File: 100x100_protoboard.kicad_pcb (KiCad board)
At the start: 2 copper layers, 0 parts

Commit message: completed first beta-version of the composite board
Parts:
- added C1: u33, Capacitors_SMD:C_0805_HandSoldering, B.Cu at (66.5, 125.2)
- added C1: u33, Capacitors_SMD:C_0805_HandSoldering, B.Cu at (107.2, 125.2)
- added C1: u33, Capacitors_SMD:C_0805_HandSoldering, B.Cu at (66.6, 33.3)
- added C1: u33, Capacitors_SMD:C_0805_HandSoldering, B.Cu at (107.2, 33.3)
- added C2: u1, Capacitors_SMD:C_0805_HandSoldering, B.Cu at (69.1, 125.2)
- added C2: u1, Capacitors_SMD:C_0805_HandSoldering, B.Cu at (104.6, 125.2)
- added C2: u1, Capacitors_SMD:C_0805_HandSoldering, B.Cu at (69.1, 33.3)
- added C2: u1, Capacitors_SMD:C_0805_HandSoldering, B.Cu at (104.6, 33.3)
- added CON1: BARREL_JACK, Connect:BARREL_JACK, B.Cu at (40.4, 125.0)
- added CON1: BARREL_JACK, Connect:BARREL_JACK, F.Cu at (133.2, 125.0)
- added CON1: BARREL_JACK, Connect:BARREL_JACK, F.Cu at (40.5, 33.5)
- added CON1: BARREL_JACK, Connect:BARREL_JACK, B.Cu at (133.3, 33.5)
- added CON2: USB_FEMALE_WITH_ID, Connectors:USB_Mini-B_Female, F.Cu at (132.0, 103.4)
- added CON2: USB_FEMALE_WITH_ID, Connectors:USB_Mini-B_Female, F.Cu at (41.8, 55.1)
- added CON3: USB_FEMALE_WITH_ID, Connectors:USB_Micro-B_Female_Wellco_AUSB_1011_05S2, B.Cu at (132.1, 103.4)
- added CON3: USB_FEMALE_WITH_ID, Connectors:USB_Micro-B_Female_Wellco_AUSB_1011_05S2, B.Cu at (41.7, 55.1)
- added F1: FUSE, Muonde:CC12ZZ, B.Cu at (51.3, 125.0)
- added F1: FUSE, Muonde:CC12ZZ, F.Cu at (122.4, 125.0)
- added F1: FUSE, Muonde:CC12ZZ, F.Cu at (51.3, 33.5)
- added F1: FUSE, Muonde:CC12ZZ, B.Cu at (122.4, 33.5)
- added F2: FUSE, Muonde:CC12ZZ, F.Cu at (51.3, 125.0)
- added F2: FUSE, Muonde:CC12ZZ, B.Cu at (122.4, 125.0)
- added F2: FUSE, Muonde:CC12ZZ, B.Cu at (51.3, 33.5)
- added F2: FUSE, Muonde:CC12ZZ, F.Cu at (122.4, 33.5)
- added GND1: INTERCONNECT_1X16, 2.54mm_Pin_Headers:Interconnect_1x16, F.Cu at (47.5, 121.2)
- added GND1: INTERCONNECT_1X16, 2.54mm_Pin_Headers:Interconnect_1x16, F.Cu at (126.2, 83.1)
- added GND1: INTERCONNECT_1X16, 2.54mm_Pin_Headers:Interconnect_1x16, F.Cu at (47.5, 75.4)
- added GND1: INTERCONNECT_1X16, 2.54mm_Pin_Headers:Interconnect_1x16, F.Cu at (126.2, 37.3)
- added GND2: INTERCONNECT_1X07, 2.54mm_Pin_Headers:Interconnect_1x07, F.Cu at (47.5, 80.5)
- added GND2: INTERCONNECT_1X07, 2.54mm_Pin_Headers:Interconnect_1x07, F.Cu at (126.2, 80.5)
- added GND2: INTERCONNECT_1X07, 2.54mm_Pin_Headers:Interconnect_1x07, F.Cu at (47.5, 78.0)
- added GND2: INTERCONNECT_1X07, 2.54mm_Pin_Headers:Interconnect_1x07, F.Cu at (126.2, 78.0)
- added GND3: INTERCONNECT_1X16, 2.54mm_Pin_Headers:Interconnect_1x16, F.Cu at (67.8, 121.2)
- added GND3: INTERCONNECT_1X16, 2.54mm_Pin_Headers:Interconnect_1x16, F.Cu at (105.9, 83.1)
- added GND3: INTERCONNECT_1X16, 2.54mm_Pin_Headers:Interconnect_1x16, F.Cu at (67.8, 75.4)
- added GND3: INTERCONNECT_1X16, 2.54mm_Pin_Headers:Interconnect_1x16, F.Cu at (105.9, 37.3)
- added GND4: INTERCONNECT_1X07, 2.54mm_Pin_Headers:Interconnect_1x07, F.Cu at (67.8, 80.5)
- added GND4: INTERCONNECT_1X07, 2.54mm_Pin_Headers:Interconnect_1x07, F.Cu at (105.9, 80.5)
- added GND4: INTERCONNECT_1X07, 2.54mm_Pin_Headers:Interconnect_1x07, F.Cu at (67.8, 78.0)
- added GND4: INTERCONNECT_1X07, 2.54mm_Pin_Headers:Interconnect_1x07, F.Cu at (105.9, 78.0)
- added J1: INTERCONNECT_1X03, 2.54mm_Pin_Headers:Interconnect_1x03, F.Cu at (50.0, 121.2)
- added J1: INTERCONNECT_1X03, 2.54mm_Pin_Headers:Interconnect_1x03, F.Cu at (123.7, 121.2)
- added J1: INTERCONNECT_1X03, 2.54mm_Pin_Headers:Interconnect_1x03, F.Cu at (50.0, 37.3)
- added J1: INTERCONNECT_1X03, 2.54mm_Pin_Headers:Interconnect_1x03, F.Cu at (123.7, 37.3)
- added J10: INTERCONNECT_1X03, 2.54mm_Pin_Headers:Interconnect_1x03, F.Cu at (50.0, 98.3)
- added J10: INTERCONNECT_1X03, 2.54mm_Pin_Headers:Interconnect_1x03, F.Cu at (123.7, 98.3)
- added J10: INTERCONNECT_1X03, 2.54mm_Pin_Headers:Interconnect_1x03, F.Cu at (50.0, 60.2)
- added J10: INTERCONNECT_1X03, 2.54mm_Pin_Headers:Interconnect_1x03, F.Cu at (123.7, 60.2)
- added J11: INTERCONNECT_1X03, 2.54mm_Pin_Headers:Interconnect_1x03, F.Cu at (50.0, 95.8)
- added J11: INTERCONNECT_1X03, 2.54mm_Pin_Headers:Interconnect_1x03, F.Cu at (123.7, 95.8)
- added J11: INTERCONNECT_1X03, 2.54mm_Pin_Headers:Interconnect_1x03, F.Cu at (50.0, 62.7)
- added J11: INTERCONNECT_1X03, 2.54mm_Pin_Headers:Interconnect_1x03, F.Cu at (123.7, 62.7)
- added J12: INTERCONNECT_1X03, 2.54mm_Pin_Headers:Interconnect_1x03, F.Cu at (50.0, 93.2)
- added J12: INTERCONNECT_1X03, 2.54mm_Pin_Headers:Interconnect_1x03, F.Cu at (123.7, 93.2)
- added J12: INTERCONNECT_1X03, 2.54mm_Pin_Headers:Interconnect_1x03, F.Cu at (50.0, 65.3)
- added J12: INTERCONNECT_1X03, 2.54mm_Pin_Headers:Interconnect_1x03, F.Cu at (123.7, 65.3)
- added J13: INTERCONNECT_1X03, 2.54mm_Pin_Headers:Interconnect_1x03, F.Cu at (50.0, 90.7)
- added J13: INTERCONNECT_1X03, 2.54mm_Pin_Headers:Interconnect_1x03, F.Cu at (123.7, 90.7)
- added J13: INTERCONNECT_1X03, 2.54mm_Pin_Headers:Interconnect_1x03, F.Cu at (50.0, 67.8)
- added J13: INTERCONNECT_1X03, 2.54mm_Pin_Headers:Interconnect_1x03, F.Cu at (123.7, 67.8)
- added J14: INTERCONNECT_1X03, 2.54mm_Pin_Headers:Interconnect_1x03, F.Cu at (50.0, 88.1)
- added J14: INTERCONNECT_1X03, 2.54mm_Pin_Headers:Interconnect_1x03, F.Cu at (123.7, 88.1)
- added J14: INTERCONNECT_1X03, 2.54mm_Pin_Headers:Interconnect_1x03, F.Cu at (50.0, 70.4)
- added J14: INTERCONNECT_1X03, 2.54mm_Pin_Headers:Interconnect_1x03, F.Cu at (123.7, 70.4)
- added J15: INTERCONNECT_1X03, 2.54mm_Pin_Headers:Interconnect_1x03, F.Cu at (50.0, 85.6)
- added J15: INTERCONNECT_1X03, 2.54mm_Pin_Headers:Interconnect_1x03, F.Cu at (123.7, 85.6)
- added J15: INTERCONNECT_1X03, 2.54mm_Pin_Headers:Interconnect_1x03, F.Cu at (50.0, 72.9)
- added J15: INTERCONNECT_1X03, 2.54mm_Pin_Headers:Interconnect_1x03, F.Cu at (123.7, 72.9)
- added J16: INTERCONNECT_1X03, 2.54mm_Pin_Headers:Interconnect_1x03, F.Cu at (50.0, 83.1)
- added J16: INTERCONNECT_1X03, 2.54mm_Pin_Headers:Interconnect_1x03, F.Cu at (123.7, 83.1)
- added J16: INTERCONNECT_1X03, 2.54mm_Pin_Headers:Interconnect_1x03, F.Cu at (50.0, 75.4)
- added J16: INTERCONNECT_1X03, 2.54mm_Pin_Headers:Interconnect_1x03, F.Cu at (123.7, 75.4)
- added J17: INTERCONNECT_1X03, 2.54mm_Pin_Headers:Interconnect_1x03, F.Cu at (57.7, 121.2)
- added J17: INTERCONNECT_1X03, 2.54mm_Pin_Headers:Interconnect_1x03, F.Cu at (116.1, 121.2)
- added J17: INTERCONNECT_1X03, 2.54mm_Pin_Headers:Interconnect_1x03, F.Cu at (57.7, 37.3)
- added J17: INTERCONNECT_1X03, 2.54mm_Pin_Headers:Interconnect_1x03, F.Cu at (116.1, 37.3)
- added J18: INTERCONNECT_1X03, 2.54mm_Pin_Headers:Interconnect_1x03, F.Cu at (57.7, 118.6)
- added J18: INTERCONNECT_1X03, 2.54mm_Pin_Headers:Interconnect_1x03, F.Cu at (116.1, 118.6)
- added J18: INTERCONNECT_1X03, 2.54mm_Pin_Headers:Interconnect_1x03, F.Cu at (57.7, 39.9)
- added J18: INTERCONNECT_1X03, 2.54mm_Pin_Headers:Interconnect_1x03, F.Cu at (116.1, 39.9)
- added J19: INTERCONNECT_1X03, 2.54mm_Pin_Headers:Interconnect_1x03, F.Cu at (57.7, 116.1)
- added J19: INTERCONNECT_1X03, 2.54mm_Pin_Headers:Interconnect_1x03, F.Cu at (116.1, 116.1)
- added J19: INTERCONNECT_1X03, 2.54mm_Pin_Headers:Interconnect_1x03, F.Cu at (57.7, 42.4)
- added J19: INTERCONNECT_1X03, 2.54mm_Pin_Headers:Interconnect_1x03, F.Cu at (116.1, 42.4)
- added J2: INTERCONNECT_1X03, 2.54mm_Pin_Headers:Interconnect_1x03, F.Cu at (50.0, 118.6)
- added J2: INTERCONNECT_1X03, 2.54mm_Pin_Headers:Interconnect_1x03, F.Cu at (123.7, 118.6)
- added J2: INTERCONNECT_1X03, 2.54mm_Pin_Headers:Interconnect_1x03, F.Cu at (50.0, 39.9)
- added J2: INTERCONNECT_1X03, 2.54mm_Pin_Headers:Interconnect_1x03, F.Cu at (123.7, 39.9)
- added J20: INTERCONNECT_1X03, 2.54mm_Pin_Headers:Interconnect_1x03, F.Cu at (57.7, 113.5)
- added J20: INTERCONNECT_1X03, 2.54mm_Pin_Headers:Interconnect_1x03, F.Cu at (116.1, 113.5)
- added J20: INTERCONNECT_1X03, 2.54mm_Pin_Headers:Interconnect_1x03, F.Cu at (57.7, 45.0)
- added J20: INTERCONNECT_1X03, 2.54mm_Pin_Headers:Interconnect_1x03, F.Cu at (116.1, 45.0)
- added J21: INTERCONNECT_1X03, 2.54mm_Pin_Headers:Interconnect_1x03, F.Cu at (57.7, 111.0)
- added J21: INTERCONNECT_1X03, 2.54mm_Pin_Headers:Interconnect_1x03, F.Cu at (116.1, 111.0)
- added J21: INTERCONNECT_1X03, 2.54mm_Pin_Headers:Interconnect_1x03, F.Cu at (57.7, 47.5)
- added J21: INTERCONNECT_1X03, 2.54mm_Pin_Headers:Interconnect_1x03, F.Cu at (116.1, 47.5)
- added J22: INTERCONNECT_1X03, 2.54mm_Pin_Headers:Interconnect_1x03, F.Cu at (57.7, 108.5)
- added J22: INTERCONNECT_1X03, 2.54mm_Pin_Headers:Interconnect_1x03, F.Cu at (116.1, 108.5)
- added J22: INTERCONNECT_1X03, 2.54mm_Pin_Headers:Interconnect_1x03, F.Cu at (57.7, 50.0)
- added J22: INTERCONNECT_1X03, 2.54mm_Pin_Headers:Interconnect_1x03, F.Cu at (116.1, 50.0)
- added J23: INTERCONNECT_1X03, 2.54mm_Pin_Headers:Interconnect_1x03, F.Cu at (57.7, 105.9)
- added J23: INTERCONNECT_1X03, 2.54mm_Pin_Headers:Interconnect_1x03, F.Cu at (116.1, 105.9)
- added J23: INTERCONNECT_1X03, 2.54mm_Pin_Headers:Interconnect_1x03, F.Cu at (57.7, 52.6)
- added J23: INTERCONNECT_1X03, 2.54mm_Pin_Headers:Interconnect_1x03, F.Cu at (116.1, 52.6)
- added J24: INTERCONNECT_1X03, 2.54mm_Pin_Headers:Interconnect_1x03, F.Cu at (57.7, 103.4)
- added J24: INTERCONNECT_1X03, 2.54mm_Pin_Headers:Interconnect_1x03, F.Cu at (116.1, 103.4)
- added J24: INTERCONNECT_1X03, 2.54mm_Pin_Headers:Interconnect_1x03, F.Cu at (57.7, 55.1)
- added J24: INTERCONNECT_1X03, 2.54mm_Pin_Headers:Interconnect_1x03, F.Cu at (116.1, 55.1)
- added J25: INTERCONNECT_1X03, 2.54mm_Pin_Headers:Interconnect_1x03, F.Cu at (57.7, 100.8)
- added J25: INTERCONNECT_1X03, 2.54mm_Pin_Headers:Interconnect_1x03, F.Cu at (116.1, 100.8)
- added J25: INTERCONNECT_1X03, 2.54mm_Pin_Headers:Interconnect_1x03, F.Cu at (57.7, 57.7)
- added J25: INTERCONNECT_1X03, 2.54mm_Pin_Headers:Interconnect_1x03, F.Cu at (116.1, 57.7)
- added J26: INTERCONNECT_1X03, 2.54mm_Pin_Headers:Interconnect_1x03, F.Cu at (57.7, 98.3)
- added J26: INTERCONNECT_1X03, 2.54mm_Pin_Headers:Interconnect_1x03, F.Cu at (116.1, 98.3)
- added J26: INTERCONNECT_1X03, 2.54mm_Pin_Headers:Interconnect_1x03, F.Cu at (57.7, 60.2)
- added J26: INTERCONNECT_1X03, 2.54mm_Pin_Headers:Interconnect_1x03, F.Cu at (116.1, 60.2)
- added J27: INTERCONNECT_1X03, 2.54mm_Pin_Headers:Interconnect_1x03, F.Cu at (57.7, 95.8)
- added J27: INTERCONNECT_1X03, 2.54mm_Pin_Headers:Interconnect_1x03, F.Cu at (116.1, 95.8)
- added J27: INTERCONNECT_1X03, 2.54mm_Pin_Headers:Interconnect_1x03, F.Cu at (57.7, 62.7)
- added J27: INTERCONNECT_1X03, 2.54mm_Pin_Headers:Interconnect_1x03, F.Cu at (116.1, 62.7)
- added J28: INTERCONNECT_1X03, 2.54mm_Pin_Headers:Interconnect_1x03, F.Cu at (57.7, 93.2)
- added J28: INTERCONNECT_1X03, 2.54mm_Pin_Headers:Interconnect_1x03, F.Cu at (116.1, 93.2)
- added J28: INTERCONNECT_1X03, 2.54mm_Pin_Headers:Interconnect_1x03, F.Cu at (57.7, 65.3)
- added J28: INTERCONNECT_1X03, 2.54mm_Pin_Headers:Interconnect_1x03, F.Cu at (116.1, 65.3)
- added J29: INTERCONNECT_1X03, 2.54mm_Pin_Headers:Interconnect_1x03, F.Cu at (57.7, 90.7)
- added J29: INTERCONNECT_1X03, 2.54mm_Pin_Headers:Interconnect_1x03, F.Cu at (116.1, 90.7)
- added J29: INTERCONNECT_1X03, 2.54mm_Pin_Headers:Interconnect_1x03, F.Cu at (57.7, 67.8)
- added J29: INTERCONNECT_1X03, 2.54mm_Pin_Headers:Interconnect_1x03, F.Cu at (116.1, 67.8)
- added J3: INTERCONNECT_1X03, 2.54mm_Pin_Headers:Interconnect_1x03, F.Cu at (50.0, 116.1)
- added J3: INTERCONNECT_1X03, 2.54mm_Pin_Headers:Interconnect_1x03, F.Cu at (123.7, 116.1)
- added J3: INTERCONNECT_1X03, 2.54mm_Pin_Headers:Interconnect_1x03, F.Cu at (50.0, 42.4)
- added J3: INTERCONNECT_1X03, 2.54mm_Pin_Headers:Interconnect_1x03, F.Cu at (123.7, 42.4)
- added J30: INTERCONNECT_1X03, 2.54mm_Pin_Headers:Interconnect_1x03, F.Cu at (57.7, 88.1)
- added J30: INTERCONNECT_1X03, 2.54mm_Pin_Headers:Interconnect_1x03, F.Cu at (116.1, 88.1)
- added J30: INTERCONNECT_1X03, 2.54mm_Pin_Headers:Interconnect_1x03, F.Cu at (57.7, 70.4)
- added J30: INTERCONNECT_1X03, 2.54mm_Pin_Headers:Interconnect_1x03, F.Cu at (116.1, 70.4)
- added J31: INTERCONNECT_1X03, 2.54mm_Pin_Headers:Interconnect_1x03, F.Cu at (57.7, 85.6)
- added J31: INTERCONNECT_1X03, 2.54mm_Pin_Headers:Interconnect_1x03, F.Cu at (116.1, 85.6)
- added J31: INTERCONNECT_1X03, 2.54mm_Pin_Headers:Interconnect_1x03, F.Cu at (57.7, 72.9)
- added J31: INTERCONNECT_1X03, 2.54mm_Pin_Headers:Interconnect_1x03, F.Cu at (116.1, 72.9)
- added J32: INTERCONNECT_1X03, 2.54mm_Pin_Headers:Interconnect_1x03, F.Cu at (57.7, 83.1)
- added J32: INTERCONNECT_1X03, 2.54mm_Pin_Headers:Interconnect_1x03, F.Cu at (116.1, 83.1)
- added J32: INTERCONNECT_1X03, 2.54mm_Pin_Headers:Interconnect_1x03, F.Cu at (57.7, 75.4)
- added J32: INTERCONNECT_1X03, 2.54mm_Pin_Headers:Interconnect_1x03, F.Cu at (116.1, 75.4)
- added J33: INTERCONNECT_1X03, 2.54mm_Pin_Headers:Interconnect_1x03, F.Cu at (70.4, 121.2)
- added J33: INTERCONNECT_1X03, 2.54mm_Pin_Headers:Interconnect_1x03, F.Cu at (103.4, 121.2)
- added J33: INTERCONNECT_1X03, 2.54mm_Pin_Headers:Interconnect_1x03, F.Cu at (70.4, 37.3)
- added J33: INTERCONNECT_1X03, 2.54mm_Pin_Headers:Interconnect_1x03, F.Cu at (103.4, 37.3)
- added J34: INTERCONNECT_1X03, 2.54mm_Pin_Headers:Interconnect_1x03, F.Cu at (70.4, 118.6)
- added J34: INTERCONNECT_1X03, 2.54mm_Pin_Headers:Interconnect_1x03, F.Cu at (103.4, 118.6)
- added J34: INTERCONNECT_1X03, 2.54mm_Pin_Headers:Interconnect_1x03, F.Cu at (70.4, 39.9)
- added J34: INTERCONNECT_1X03, 2.54mm_Pin_Headers:Interconnect_1x03, F.Cu at (103.4, 39.9)
- added J35: INTERCONNECT_1X03, 2.54mm_Pin_Headers:Interconnect_1x03, F.Cu at (70.4, 116.1)
- added J35: INTERCONNECT_1X03, 2.54mm_Pin_Headers:Interconnect_1x03, F.Cu at (103.4, 116.1)
- added J35: INTERCONNECT_1X03, 2.54mm_Pin_Headers:Interconnect_1x03, F.Cu at (70.4, 42.4)
- added J35: INTERCONNECT_1X03, 2.54mm_Pin_Headers:Interconnect_1x03, F.Cu at (103.4, 42.4)
- added J36: INTERCONNECT_1X03, 2.54mm_Pin_Headers:Interconnect_1x03, F.Cu at (70.4, 113.5)
- added J36: INTERCONNECT_1X03, 2.54mm_Pin_Headers:Interconnect_1x03, F.Cu at (103.4, 113.5)
- added J36: INTERCONNECT_1X03, 2.54mm_Pin_Headers:Interconnect_1x03, F.Cu at (70.4, 45.0)
- added J36: INTERCONNECT_1X03, 2.54mm_Pin_Headers:Interconnect_1x03, F.Cu at (103.4, 45.0)
- added J37: INTERCONNECT_1X03, 2.54mm_Pin_Headers:Interconnect_1x03, F.Cu at (70.4, 111.0)
- added J37: INTERCONNECT_1X03, 2.54mm_Pin_Headers:Interconnect_1x03, F.Cu at (103.4, 111.0)
- added J37: INTERCONNECT_1X03, 2.54mm_Pin_Headers:Interconnect_1x03, F.Cu at (70.4, 47.5)
- added J37: INTERCONNECT_1X03, 2.54mm_Pin_Headers:Interconnect_1x03, F.Cu at (103.4, 47.5)
- added J38: INTERCONNECT_1X03, 2.54mm_Pin_Headers:Interconnect_1x03, F.Cu at (70.4, 108.5)
- added J38: INTERCONNECT_1X03, 2.54mm_Pin_Headers:Interconnect_1x03, F.Cu at (103.4, 108.5)
- added J38: INTERCONNECT_1X03, 2.54mm_Pin_Headers:Interconnect_1x03, F.Cu at (70.4, 50.0)
- added J38: INTERCONNECT_1X03, 2.54mm_Pin_Headers:Interconnect_1x03, F.Cu at (103.4, 50.0)
- added J39: INTERCONNECT_1X03, 2.54mm_Pin_Headers:Interconnect_1x03, F.Cu at (70.4, 105.9)
- added J39: INTERCONNECT_1X03, 2.54mm_Pin_Headers:Interconnect_1x03, F.Cu at (103.4, 105.9)
- added J39: INTERCONNECT_1X03, 2.54mm_Pin_Headers:Interconnect_1x03, F.Cu at (70.4, 52.6)
- added J39: INTERCONNECT_1X03, 2.54mm_Pin_Headers:Interconnect_1x03, F.Cu at (103.4, 52.6)
- added J4: INTERCONNECT_1X03, 2.54mm_Pin_Headers:Interconnect_1x03, F.Cu at (50.0, 113.5)
- added J4: INTERCONNECT_1X03, 2.54mm_Pin_Headers:Interconnect_1x03, F.Cu at (123.7, 113.5)
- added J4: INTERCONNECT_1X03, 2.54mm_Pin_Headers:Interconnect_1x03, F.Cu at (50.0, 45.0)
- added J4: INTERCONNECT_1X03, 2.54mm_Pin_Headers:Interconnect_1x03, F.Cu at (123.7, 45.0)
- added J40: INTERCONNECT_1X03, 2.54mm_Pin_Headers:Interconnect_1x03, F.Cu at (70.4, 103.4)
- added J40: INTERCONNECT_1X03, 2.54mm_Pin_Headers:Interconnect_1x03, F.Cu at (103.4, 103.4)
- added J40: INTERCONNECT_1X03, 2.54mm_Pin_Headers:Interconnect_1x03, F.Cu at (70.4, 55.1)
- added J40: INTERCONNECT_1X03, 2.54mm_Pin_Headers:Interconnect_1x03, F.Cu at (103.4, 55.1)
- added J41: INTERCONNECT_1X03, 2.54mm_Pin_Headers:Interconnect_1x03, F.Cu at (70.4, 100.8)
- added J41: INTERCONNECT_1X03, 2.54mm_Pin_Headers:Interconnect_1x03, F.Cu at (103.4, 100.8)
- added J41: INTERCONNECT_1X03, 2.54mm_Pin_Headers:Interconnect_1x03, F.Cu at (70.4, 57.7)
- added J41: INTERCONNECT_1X03, 2.54mm_Pin_Headers:Interconnect_1x03, F.Cu at (103.4, 57.7)
- added J42: INTERCONNECT_1X03, 2.54mm_Pin_Headers:Interconnect_1x03, F.Cu at (70.4, 98.3)
- added J42: INTERCONNECT_1X03, 2.54mm_Pin_Headers:Interconnect_1x03, F.Cu at (103.4, 98.3)
- added J42: INTERCONNECT_1X03, 2.54mm_Pin_Headers:Interconnect_1x03, F.Cu at (70.4, 60.2)
- added J42: INTERCONNECT_1X03, 2.54mm_Pin_Headers:Interconnect_1x03, F.Cu at (103.4, 60.2)
- added J43: INTERCONNECT_1X03, 2.54mm_Pin_Headers:Interconnect_1x03, F.Cu at (70.4, 95.8)
- added J43: INTERCONNECT_1X03, 2.54mm_Pin_Headers:Interconnect_1x03, F.Cu at (103.4, 95.8)
- added J43: INTERCONNECT_1X03, 2.54mm_Pin_Headers:Interconnect_1x03, F.Cu at (70.4, 62.7)
- added J43: INTERCONNECT_1X03, 2.54mm_Pin_Headers:Interconnect_1x03, F.Cu at (103.4, 62.7)
- added J44: INTERCONNECT_1X03, 2.54mm_Pin_Headers:Interconnect_1x03, F.Cu at (70.4, 93.2)
- added J44: INTERCONNECT_1X03, 2.54mm_Pin_Headers:Interconnect_1x03, F.Cu at (103.4, 93.2)
- added J44: INTERCONNECT_1X03, 2.54mm_Pin_Headers:Interconnect_1x03, F.Cu at (70.4, 65.3)
- added J44: INTERCONNECT_1X03, 2.54mm_Pin_Headers:Interconnect_1x03, F.Cu at (103.4, 65.3)
- added J45: INTERCONNECT_1X03, 2.54mm_Pin_Headers:Interconnect_1x03, F.Cu at (70.4, 90.7)
- added J45: INTERCONNECT_1X03, 2.54mm_Pin_Headers:Interconnect_1x03, F.Cu at (103.4, 90.7)
- added J45: INTERCONNECT_1X03, 2.54mm_Pin_Headers:Interconnect_1x03, F.Cu at (70.4, 67.8)
- added J45: INTERCONNECT_1X03, 2.54mm_Pin_Headers:Interconnect_1x03, F.Cu at (103.4, 67.8)
- added J46: INTERCONNECT_1X03, 2.54mm_Pin_Headers:Interconnect_1x03, F.Cu at (70.4, 88.1)
- added J46: INTERCONNECT_1X03, 2.54mm_Pin_Headers:Interconnect_1x03, F.Cu at (103.4, 88.1)
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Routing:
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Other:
- board outline added: 97.8 x 96.5 mm
- net class Power added: clearance 0.254, trace_width 2.032, via_dia 0.889, via_drill 0.635
- board text added: "100n"
- board text added: "330n"
- board text added: "78 XX"
- board text added: "D+"
- board text added: "D-"
- board text added: "FUSE"
- board text added: "GND"
- board text added: "ID"
- board text added: "POWER JACK"
- board text added: "PTC"
- board text added: "USB MICRO"
- board text added: "USB MINI"
- board text added: "VCC"

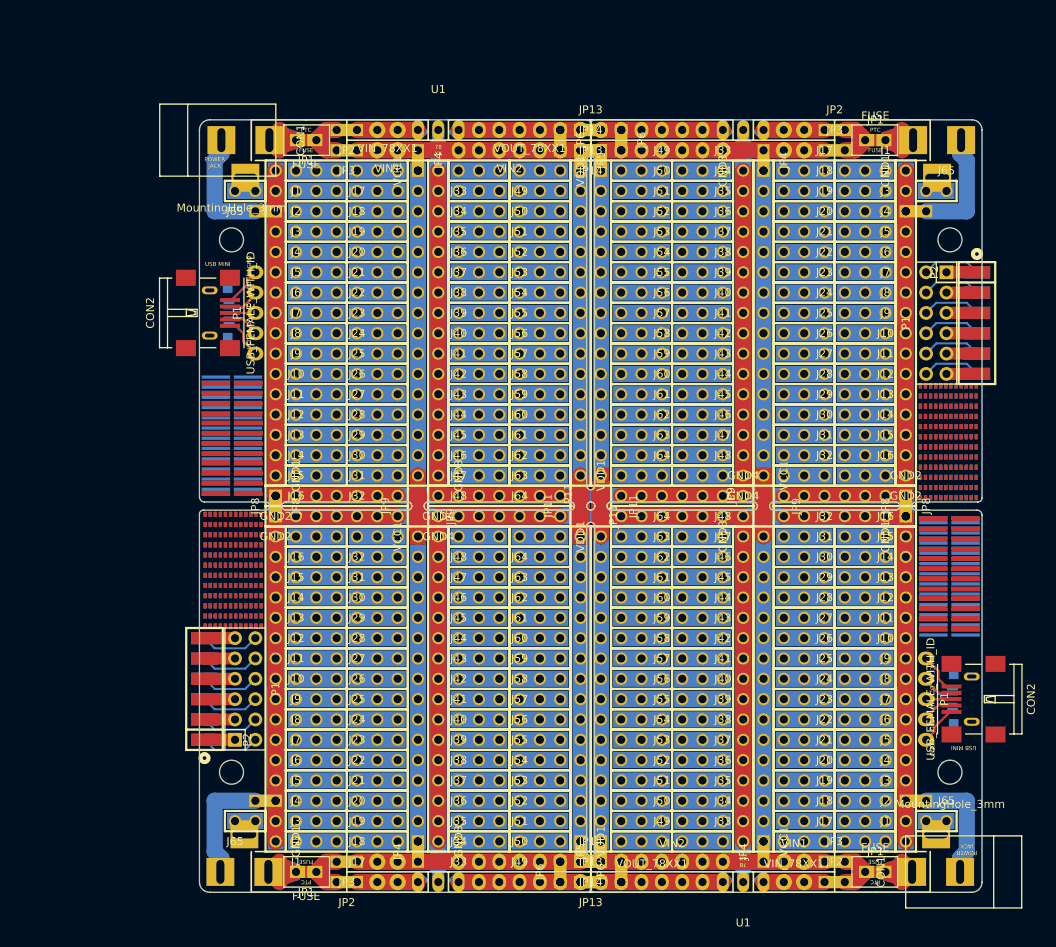
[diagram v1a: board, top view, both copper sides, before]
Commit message: moved shorted inter-board GND connection to center, switched av from Oddities:NetTie-I_Connected_SMD because they were asymmetrical and fixed pin header outlines
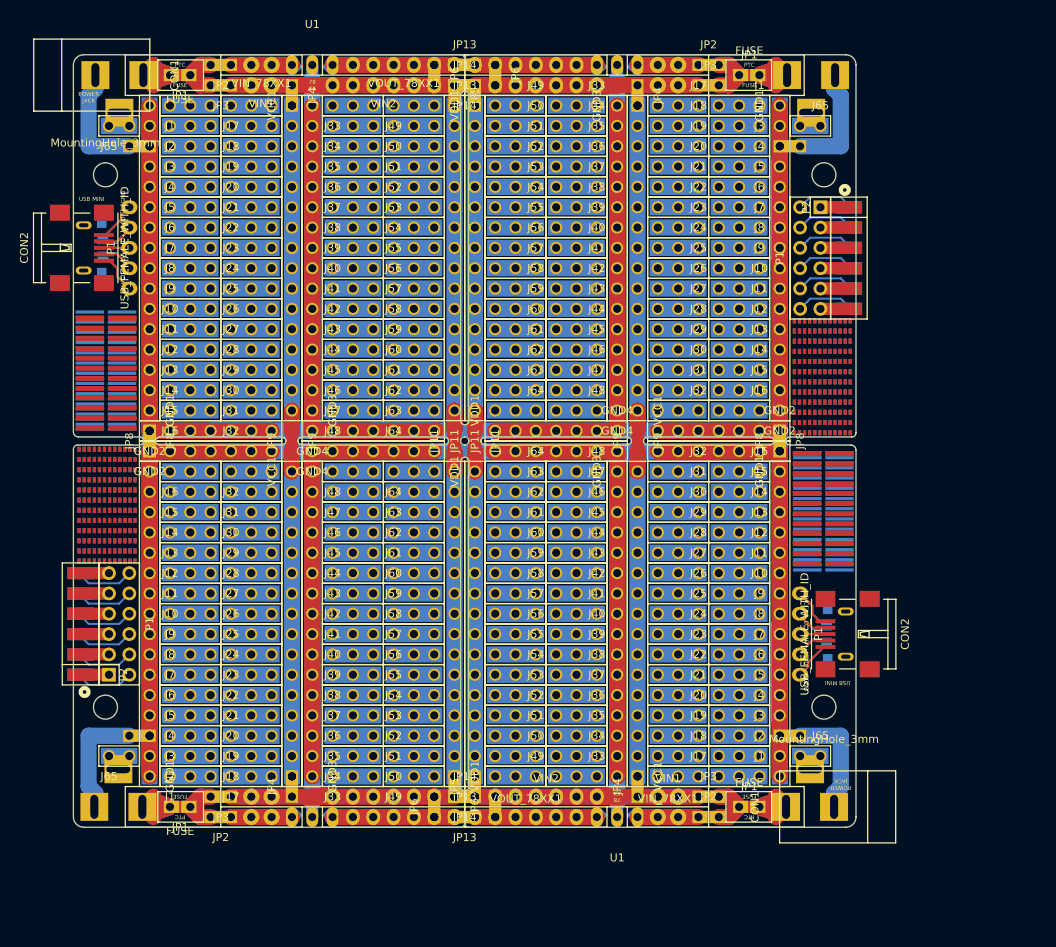
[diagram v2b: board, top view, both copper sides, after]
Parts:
- removed the C1 at (66.5, 125.2)
- removed the C1 at (107.2, 125.2)
- removed the C1 at (66.6, 33.3)
- removed the C1 at (107.2, 33.3)
- removed the C2 at (69.1, 125.2)
- removed the C2 at (104.6, 125.2)
- removed the C2 at (69.1, 33.3)
- removed the C2 at (104.6, 33.3)
- removed the CON1 at (40.4, 125.0)
- removed the CON1 at (133.2, 125.0)
- removed the CON1 at (40.5, 33.5)
- removed the CON1 at (133.3, 33.5)
- removed the CON2 at (132.0, 103.4)
- removed the CON2 at (41.8, 55.1)
- removed the CON3 at (132.1, 103.4)
- removed the CON3 at (41.7, 55.1)
- removed the F1 at (51.3, 125.0)
- removed the F1 at (122.4, 125.0)
- removed the F1 at (51.3, 33.5)
- removed the F1 at (122.4, 33.5)
- removed the F2 at (51.3, 125.0)
- removed the F2 at (122.4, 125.0)
- removed the F2 at (51.3, 33.5)
- removed the F2 at (122.4, 33.5)
- removed the GND1 at (47.5, 121.2)
- removed the GND1 at (126.2, 83.1)
- removed the GND1 at (47.5, 75.4)
- removed the GND1 at (126.2, 37.3)
- removed the GND2 at (47.5, 80.5)
- removed the GND2 at (126.2, 80.5)
- removed the GND2 at (47.5, 78.0)
- removed the GND2 at (126.2, 78.0)
- removed the GND3 at (67.8, 121.2)
- removed the GND3 at (105.9, 83.1)
- removed the GND3 at (67.8, 75.4)
- removed the GND3 at (105.9, 37.3)
- removed the GND4 at (67.8, 80.5)
- removed the GND4 at (105.9, 80.5)
- removed the GND4 at (67.8, 78.0)
- removed the GND4 at (105.9, 78.0)
- removed the J1 at (50.0, 121.2)
- removed the J1 at (123.7, 121.2)
- removed the J1 at (50.0, 37.3)
- removed the J1 at (123.7, 37.3)
- removed the J10 at (50.0, 98.3)
- removed the J10 at (123.7, 98.3)
- removed the J10 at (50.0, 60.2)
- removed the J10 at (123.7, 60.2)
- removed the J11 at (50.0, 95.8)
- removed the J11 at (123.7, 95.8)
- removed the J11 at (50.0, 62.7)
- removed the J11 at (123.7, 62.7)
- removed the J12 at (50.0, 93.2)
- removed the J12 at (123.7, 93.2)
- removed the J12 at (50.0, 65.3)
- removed the J12 at (123.7, 65.3)
- removed the J13 at (50.0, 90.7)
- removed the J13 at (123.7, 90.7)
- removed the J13 at (50.0, 67.8)
- removed the J13 at (123.7, 67.8)
- removed the J14 at (50.0, 88.1)
- removed the J14 at (123.7, 88.1)
- removed the J14 at (50.0, 70.4)
- removed the J14 at (123.7, 70.4)
- removed the J15 at (50.0, 85.6)
- removed the J15 at (123.7, 85.6)
- removed the J15 at (50.0, 72.9)
- removed the J15 at (123.7, 72.9)
- removed the J16 at (50.0, 83.1)
- removed the J16 at (123.7, 83.1)
- removed the J16 at (50.0, 75.4)
- removed the J16 at (123.7, 75.4)
- removed the J17 at (57.7, 121.2)
- removed the J17 at (116.1, 121.2)
- removed the J17 at (57.7, 37.3)
- removed the J17 at (116.1, 37.3)
- removed the J18 at (57.7, 118.6)
- removed the J18 at (116.1, 118.6)
- removed the J18 at (57.7, 39.9)
- removed the J18 at (116.1, 39.9)
- removed the J19 at (57.7, 116.1)
- removed the J19 at (116.1, 116.1)
- removed the J19 at (57.7, 42.4)
- removed the J19 at (116.1, 42.4)
- removed the J2 at (50.0, 118.6)
- removed the J2 at (123.7, 118.6)
- removed the J2 at (50.0, 39.9)
- removed the J2 at (123.7, 39.9)
- removed the J20 at (57.7, 113.5)
- removed the J20 at (116.1, 113.5)
- removed the J20 at (57.7, 45.0)
- removed the J20 at (116.1, 45.0)
- removed the J21 at (57.7, 111.0)
- removed the J21 at (116.1, 111.0)
- removed the J21 at (57.7, 47.5)
- removed the J21 at (116.1, 47.5)
- removed the J22 at (57.7, 108.5)
- removed the J22 at (116.1, 108.5)
- removed the J22 at (57.7, 50.0)
- removed the J22 at (116.1, 50.0)
- removed the J23 at (57.7, 105.9)
- removed the J23 at (116.1, 105.9)
- removed the J23 at (57.7, 52.6)
- removed the J23 at (116.1, 52.6)
- removed the J24 at (57.7, 103.4)
- removed the J24 at (116.1, 103.4)
- removed the J24 at (57.7, 55.1)
- removed the J24 at (116.1, 55.1)
- removed the J25 at (57.7, 100.8)
- removed the J25 at (116.1, 100.8)
- removed the J25 at (57.7, 57.7)
- removed the J25 at (116.1, 57.7)
- removed the J26 at (57.7, 98.3)
- removed the J26 at (116.1, 98.3)
- removed the J26 at (57.7, 60.2)
- removed the J26 at (116.1, 60.2)
- removed the J27 at (57.7, 95.8)
- removed the J27 at (116.1, 95.8)
- removed the J27 at (57.7, 62.7)
- removed the J27 at (116.1, 62.7)
- removed the J28 at (57.7, 93.2)
- removed the J28 at (116.1, 93.2)
- removed the J28 at (57.7, 65.3)
- removed the J28 at (116.1, 65.3)
- removed the J29 at (57.7, 90.7)
- removed the J29 at (116.1, 90.7)
- removed the J29 at (57.7, 67.8)
- removed the J29 at (116.1, 67.8)
- removed the J3 at (50.0, 116.1)
- removed the J3 at (123.7, 116.1)
- removed the J3 at (50.0, 42.4)
- removed the J3 at (123.7, 42.4)
- removed the J30 at (57.7, 88.1)
- removed the J30 at (116.1, 88.1)
- removed the J30 at (57.7, 70.4)
- removed the J30 at (116.1, 70.4)
- removed the J31 at (57.7, 85.6)
- removed the J31 at (116.1, 85.6)
- removed the J31 at (57.7, 72.9)
- removed the J31 at (116.1, 72.9)
- removed the J32 at (57.7, 83.1)
- removed the J32 at (116.1, 83.1)
- removed the J32 at (57.7, 75.4)
- removed the J32 at (116.1, 75.4)
- removed the J33 at (70.4, 121.2)
- removed the J33 at (103.4, 121.2)
- removed the J33 at (70.4, 37.3)
- removed the J33 at (103.4, 37.3)
- removed the J34 at (70.4, 118.6)
- removed the J34 at (103.4, 118.6)
- removed the J34 at (70.4, 39.9)
- removed the J34 at (103.4, 39.9)
- removed the J35 at (70.4, 116.1)
- removed the J35 at (103.4, 116.1)
- removed the J35 at (70.4, 42.4)
- removed the J35 at (103.4, 42.4)
- removed the J36 at (70.4, 113.5)
- removed the J36 at (103.4, 113.5)
- removed the J36 at (70.4, 45.0)
- removed the J36 at (103.4, 45.0)
- removed the J37 at (70.4, 111.0)
- removed the J37 at (103.4, 111.0)
- removed the J37 at (70.4, 47.5)
- removed the J37 at (103.4, 47.5)
- removed the J38 at (70.4, 108.5)
- removed the J38 at (103.4, 108.5)
- removed the J38 at (70.4, 50.0)
- removed the J38 at (103.4, 50.0)
- removed the J39 at (70.4, 105.9)
- removed the J39 at (103.4, 105.9)
- removed the J39 at (70.4, 52.6)
- removed the J39 at (103.4, 52.6)
- removed the J4 at (50.0, 113.5)
- removed the J4 at (123.7, 113.5)
- removed the J4 at (50.0, 45.0)
- removed the J4 at (123.7, 45.0)
- removed the J40 at (70.4, 103.4)
- removed the J40 at (103.4, 103.4)
- removed the J40 at (70.4, 55.1)
- removed the J40 at (103.4, 55.1)
- removed the J41 at (70.4, 100.8)
- removed the J41 at (103.4, 100.8)
- removed the J41 at (70.4, 57.7)
- removed the J41 at (103.4, 57.7)
- removed the J42 at (70.4, 98.3)
- removed the J42 at (103.4, 98.3)
- removed the J42 at (70.4, 60.2)
- removed the J42 at (103.4, 60.2)
- removed the J43 at (70.4, 95.8)
- removed the J43 at (103.4, 95.8)
- removed the J43 at (70.4, 62.7)
- removed the J43 at (103.4, 62.7)
- removed the J44 at (70.4, 93.2)
- removed the J44 at (103.4, 93.2)
- removed the J44 at (70.4, 65.3)
- removed the J44 at (103.4, 65.3)
- removed the J45 at (70.4, 90.7)
- removed the J45 at (103.4, 90.7)
- removed the J45 at (70.4, 67.8)
- removed the J45 at (103.4, 67.8)
- removed the J46 at (70.4, 88.1)
- removed the J46 at (103.4, 88.1)
- removed the J46 at (70.4, 70.4)
- removed the J46 at (103.4, 70.4)
- removed the J47 at (70.4, 85.6)
- removed the J47 at (103.4, 85.6)
- removed the J47 at (70.4, 72.9)
- removed the J47 at (103.4, 72.9)
- removed the J48 at (70.4, 83.1)
- removed the J48 at (103.4, 83.1)
- removed the J48 at (70.4, 75.4)
- removed the J48 at (103.4, 75.4)
- removed the J49 at (78.0, 121.2)
- removed the J49 at (95.8, 121.2)
- removed the J49 at (78.0, 37.3)
- removed the J49 at (95.8, 37.3)
- removed the J5 at (50.0, 111.0)
- removed the J5 at (123.7, 111.0)
- removed the J5 at (50.0, 47.5)
- removed the J5 at (123.7, 47.5)
- removed the J50 at (78.0, 118.6)
- removed the J50 at (95.8, 118.6)
- removed the J50 at (78.0, 39.9)
- removed the J50 at (95.8, 39.9)
- removed the J51 at (78.0, 116.1)
- removed the J51 at (95.8, 116.1)
- removed the J51 at (78.0, 42.4)
- removed the J51 at (95.8, 42.4)
- removed the J52 at (78.0, 113.5)
- removed the J52 at (95.8, 113.5)
- removed the J52 at (78.0, 45.0)
- removed the J52 at (95.8, 45.0)
- removed the J53 at (78.0, 111.0)
- removed the J53 at (95.8, 111.0)
- removed the J53 at (78.0, 47.5)
- removed the J53 at (95.8, 47.5)
- removed the J54 at (78.0, 108.5)
- removed the J54 at (95.8, 108.5)
- removed the J54 at (78.0, 50.0)
- removed the J54 at (95.8, 50.0)
- removed the J55 at (78.0, 105.9)
- removed the J55 at (95.8, 105.9)
- removed the J55 at (78.0, 52.6)
- removed the J55 at (95.8, 52.6)
- removed the J56 at (78.0, 103.4)
- removed the J56 at (95.8, 103.4)
- removed the J56 at (78.0, 55.1)
- removed the J56 at (95.8, 55.1)
- removed the J57 at (78.0, 100.8)
- removed the J57 at (95.8, 100.8)
- removed the J57 at (78.0, 57.7)
- removed the J57 at (95.8, 57.7)
- removed the J58 at (78.0, 98.3)
- removed the J58 at (95.8, 98.3)
- removed the J58 at (78.0, 60.2)
- removed the J58 at (95.8, 60.2)
- removed the J59 at (78.0, 95.8)
- removed the J59 at (95.8, 95.8)
- removed the J59 at (78.0, 62.7)
- removed the J59 at (95.8, 62.7)
- removed the J6 at (50.0, 108.5)
- removed the J6 at (123.7, 108.5)
- removed the J6 at (50.0, 50.0)
- removed the J6 at (123.7, 50.0)
- removed the J60 at (78.0, 93.2)
- removed the J60 at (95.8, 93.2)
- removed the J60 at (78.0, 65.3)
- removed the J60 at (95.8, 65.3)
- removed the J61 at (78.0, 90.7)
- removed the J61 at (95.8, 90.7)
- removed the J61 at (78.0, 67.8)
- removed the J61 at (95.8, 67.8)
- removed the J62 at (78.0, 88.1)
- removed the J62 at (95.8, 88.1)
- removed the J62 at (78.0, 70.4)
- removed the J62 at (95.8, 70.4)
- removed the J63 at (78.0, 85.6)
- removed the J63 at (95.8, 85.6)
- removed the J63 at (78.0, 72.9)
- removed the J63 at (95.8, 72.9)
- removed the J64 at (78.0, 83.1)
- removed the J64 at (95.8, 83.1)
- removed the J64 at (78.0, 75.4)
- removed the J64 at (95.8, 75.4)
- removed the J65 at (42.4, 118.6)
- removed the J65 at (131.3, 118.6)
- removed the J65 at (42.4, 39.9)
- removed the J65 at (131.3, 39.9)
- removed the J7 at (50.0, 105.9)
- removed the J7 at (123.7, 105.9)
- removed the J7 at (50.0, 52.6)
- removed the J7 at (123.7, 52.6)
- removed the J8 at (50.0, 103.4)
- removed the J8 at (123.7, 103.4)
- removed the J8 at (50.0, 55.1)
- removed the J8 at (123.7, 55.1)
- removed the J9 at (50.0, 100.8)
- removed the J9 at (123.7, 100.8)
- removed the J9 at (50.0, 57.7)
- removed the J9 at (123.7, 57.7)
- removed the JP1 at (51.3, 125.0)
- removed the JP1 at (122.4, 125.0)
- removed the JP1 at (51.3, 33.5)
- removed the JP1 at (122.4, 33.5)
- removed the JP10 at (85.6, 79.2) (x2)
- removed the JP10 at (88.1, 79.2) (x2)
- removed the JP11 at (85.6, 80.5)
- removed the JP11 at (88.1, 79.2)
- removed the JP11 at (85.6, 79.2)
- removed the JP11 at (88.1, 78.0)
- removed the JP12 at (86.9, 80.5) (x2)
- removed the JP12 at (86.9, 78.0) (x2)
- removed the JP13 at (86.9, 126.2) (x2)
- removed the JP13 at (86.9, 32.3) (x2)
- removed the JP14 at (86.9, 123.7) (x2)
- removed the JP14 at (86.9, 34.8) (x2)
- removed the JP15 at (65.3, 79.2) (x2)
- removed the JP15 at (108.5, 79.2) (x2)
- removed the JP2 at (56.4, 126.2)
- removed the JP2 at (117.3, 126.2)
- removed the JP2 at (56.4, 32.3)
- removed the JP2 at (117.3, 32.3)
- removed the JP3 at (56.4, 123.7)
- removed the JP3 at (117.3, 123.7)
- removed the JP3 at (56.4, 34.8)
- removed the JP3 at (117.3, 34.8)
- removed the JP4 at (65.3, 122.4)
- removed the JP4 at (108.5, 122.4)
- removed the JP4 at (65.3, 36.1)
- removed the JP4 at (108.5, 36.1)
- removed the JP5 at (85.6, 122.4)
- removed the JP5 at (88.1, 122.4)
- removed the JP5 at (85.6, 36.1)
- removed the JP5 at (88.1, 36.1)
- removed the JP6 at (83.1, 125.0)
- removed the JP6 at (90.7, 125.0)
- removed the JP6 at (83.1, 33.5)
- removed the JP6 at (90.7, 33.5)
- removed the JP7 at (46.2, 116.1)
- removed the JP7 at (127.5, 116.1)
- removed the JP7 at (46.2, 42.4)
- removed the JP7 at (127.5, 42.4)
- removed the JP8 at (47.5, 79.2) (x2)
- removed the JP8 at (126.2, 79.2) (x2)
- removed the JP9 at (65.3, 80.5)
- removed the JP9 at (108.5, 79.2)
- removed the JP9 at (65.3, 79.2)
- removed the JP9 at (108.5, 78.0)
- removed the MountingHole_3mm at (42.0, 112.5)
- removed the MountingHole_3mm at (131.8, 112.5)
- removed the MountingHole_3mm at (42.0, 46.0)
- removed the MountingHole_3mm at (131.8, 46.0)
- removed the P1 at (43.7, 102.1)
- removed the P1 at (128.8, 103.4)
- removed the P1 at (45.0, 55.1)
- removed the P1 at (130.0, 56.4)
- removed the P2 at (38.6, 108.5)
- removed the P2 at (135.1, 50.0)
- removed the Ref** at (41.5, 92.4) (x2)
- removed the Ref** at (131.7, 82.9)
- removed the Ref** at (131.7, 88.0)
- removed the Ref** at (131.7, 93.1)
- removed the Ref** at (42.0, 65.4)
- removed the Ref** at (42.0, 70.5)
- removed the Ref** at (42.0, 75.6)
- removed the Ref** at (42.1, 75.7)
- removed the Ref** at (42.1, 70.8)
- removed the Ref** at (42.1, 65.8)
- removed the Ref** at (132.2, 76.3) (x2)
- removed the Ref** at (41.5, 87.3) (x2)
- removed the Ref** at (132.2, 71.2) (x2)
- removed the Ref** at (132.2, 66.1) (x2)
- removed the Ref** at (41.5, 82.2) (x2)
- removed the Ref** at (131.7, 92.7)
- removed the Ref** at (131.7, 87.7)
- removed the Ref** at (131.7, 82.8)
- removed the U1 at (67.8, 126.2)
- removed the U1 at (105.9, 126.2)
- removed the U1 at (67.8, 32.3)
- removed the U1 at (105.9, 32.3)
- removed the VCC1 at (65.3, 83.1)
- removed the VCC1 at (108.5, 121.2)
- removed the VCC1 at (65.3, 37.3)
- removed the VCC1 at (108.5, 75.4)
- removed the VDD1 at (85.6, 121.2)
- removed the VDD1 at (88.1, 83.1)
- removed the VDD1 at (85.6, 75.4)
- removed the VDD1 at (88.1, 37.3)
- removed the VIN1 at (61.5, 123.7)
- removed the VIN1 at (112.3, 123.7)
- removed the VIN1 at (61.5, 34.8)
- removed the VIN1 at (112.3, 34.8)
- removed the VIN2 at (76.7, 123.7)
- removed the VIN2 at (97.0, 123.7)
- removed the VIN2 at (76.7, 34.8)
- removed the VIN2 at (97.0, 34.8)
- removed the VIN_78XX1 at (61.5, 126.2)
- removed the VIN_78XX1 at (112.3, 126.2)
- removed the VIN_78XX1 at (61.5, 32.3)
- removed the VIN_78XX1 at (112.3, 32.3)
- removed the VOUT_78XX1 at (79.2, 126.2)
- removed the VOUT_78XX1 at (94.5, 126.2)
- removed the VOUT_78XX1 at (79.2, 32.3)
- removed the VOUT_78XX1 at (94.5, 32.3)
- added C1: u33, Capacitors_SMD:C_0805_HandSoldering, B.Cu at (50.8, 117.1)
- added C1: u33, Capacitors_SMD:C_0805_HandSoldering, B.Cu at (91.4, 117.1)
- added C1: u33, Capacitors_SMD:C_0805_HandSoldering, B.Cu at (50.8, 25.1)
- added C1: u33, Capacitors_SMD:C_0805_HandSoldering, B.Cu at (91.4, 25.1)
- added C2: u1, Capacitors_SMD:C_0805_HandSoldering, B.Cu at (53.3, 117.1)
- added C2: u1, Capacitors_SMD:C_0805_HandSoldering, B.Cu at (88.9, 117.1)
- added C2: u1, Capacitors_SMD:C_0805_HandSoldering, B.Cu at (53.3, 25.1)
- added C2: u1, Capacitors_SMD:C_0805_HandSoldering, B.Cu at (88.9, 25.1)
- added CON1: BARREL_JACK, Connect:BARREL_JACK, B.Cu at (24.6, 116.8)
- added CON1: BARREL_JACK, Connect:BARREL_JACK, F.Cu at (117.5, 116.8)
- added CON1: BARREL_JACK, Connect:BARREL_JACK, F.Cu at (24.8, 25.4)
- added CON1: BARREL_JACK, Connect:BARREL_JACK, B.Cu at (117.6, 25.4)
- added CON2: USB_FEMALE_WITH_ID, Connectors:USB_Mini-B_Female, F.Cu at (116.2, 95.2)
- added CON2: USB_FEMALE_WITH_ID, Connectors:USB_Mini-B_Female, F.Cu at (26.0, 47.0)
- added CON3: USB_FEMALE_WITH_ID, Connectors:USB_Micro-B_Female_Wellco_AUSB_1011_05S2, B.Cu at (116.3, 95.2)
- added CON3: USB_FEMALE_WITH_ID, Connectors:USB_Micro-B_Female_Wellco_AUSB_1011_05S2, B.Cu at (25.9, 47.0)
- added F1: FUSE, Muonde:CC12ZZ, B.Cu at (35.6, 116.8)
- added F1: FUSE, Muonde:CC12ZZ, F.Cu at (106.7, 116.8)
- added F1: FUSE, Muonde:CC12ZZ, F.Cu at (35.6, 25.4)
- added F1: FUSE, Muonde:CC12ZZ, B.Cu at (106.7, 25.4)
- added F2: FUSE, Muonde:CC12ZZ, F.Cu at (35.6, 116.8)
- added F2: FUSE, Muonde:CC12ZZ, B.Cu at (106.7, 116.8)
- added F2: FUSE, Muonde:CC12ZZ, B.Cu at (35.6, 25.4)
- added F2: FUSE, Muonde:CC12ZZ, F.Cu at (106.7, 25.4)
- added GND1: INTERCONNECT_1X16, 2.54mm_Pin_Headers:Interconnect_1x16, F.Cu at (31.8, 113.0)
- added GND1: INTERCONNECT_1X16, 2.54mm_Pin_Headers:Interconnect_1x16, F.Cu at (110.5, 74.9)
- added GND1: INTERCONNECT_1X16, 2.54mm_Pin_Headers:Interconnect_1x16, F.Cu at (31.8, 67.3)
- added GND1: INTERCONNECT_1X16, 2.54mm_Pin_Headers:Interconnect_1x16, F.Cu at (110.5, 29.2)
- added GND2: INTERCONNECT_1X07, 2.54mm_Pin_Headers:Interconnect_1x07, F.Cu at (31.8, 72.4)
- added GND2: INTERCONNECT_1X07, 2.54mm_Pin_Headers:Interconnect_1x07, F.Cu at (110.5, 72.4)
- added GND2: INTERCONNECT_1X07, 2.54mm_Pin_Headers:Interconnect_1x07, F.Cu at (31.8, 69.8)
- added GND2: INTERCONNECT_1X07, 2.54mm_Pin_Headers:Interconnect_1x07, F.Cu at (110.5, 69.8)
- added GND3: INTERCONNECT_1X16, 2.54mm_Pin_Headers:Interconnect_1x16, F.Cu at (52.1, 113.0)
- added GND3: INTERCONNECT_1X16, 2.54mm_Pin_Headers:Interconnect_1x16, F.Cu at (90.2, 74.9)
- added GND3: INTERCONNECT_1X16, 2.54mm_Pin_Headers:Interconnect_1x16, F.Cu at (52.1, 67.3)
- added GND3: INTERCONNECT_1X16, 2.54mm_Pin_Headers:Interconnect_1x16, F.Cu at (90.2, 29.2)
- added GND4: INTERCONNECT_1X07, 2.54mm_Pin_Headers:Interconnect_1x07, F.Cu at (52.1, 72.4)
- added GND4: INTERCONNECT_1X07, 2.54mm_Pin_Headers:Interconnect_1x07, F.Cu at (90.2, 72.4)
- added GND4: INTERCONNECT_1X07, 2.54mm_Pin_Headers:Interconnect_1x07, F.Cu at (52.1, 69.8)
- added GND4: INTERCONNECT_1X07, 2.54mm_Pin_Headers:Interconnect_1x07, F.Cu at (90.2, 69.8)
- added J1: INTERCONNECT_1X03, 2.54mm_Pin_Headers:Interconnect_1x03, F.Cu at (34.3, 113.0)
- added J1: INTERCONNECT_1X03, 2.54mm_Pin_Headers:Interconnect_1x03, F.Cu at (108.0, 113.0)
- added J1: INTERCONNECT_1X03, 2.54mm_Pin_Headers:Interconnect_1x03, F.Cu at (34.3, 29.2)
- added J1: INTERCONNECT_1X03, 2.54mm_Pin_Headers:Interconnect_1x03, F.Cu at (108.0, 29.2)
- added J10: INTERCONNECT_1X03, 2.54mm_Pin_Headers:Interconnect_1x03, F.Cu at (34.3, 90.2)
- added J10: INTERCONNECT_1X03, 2.54mm_Pin_Headers:Interconnect_1x03, F.Cu at (108.0, 90.2)
- added J10: INTERCONNECT_1X03, 2.54mm_Pin_Headers:Interconnect_1x03, F.Cu at (34.3, 52.1)
- added J10: INTERCONNECT_1X03, 2.54mm_Pin_Headers:Interconnect_1x03, F.Cu at (108.0, 52.1)
- added J11: INTERCONNECT_1X03, 2.54mm_Pin_Headers:Interconnect_1x03, F.Cu at (34.3, 87.6)
- added J11: INTERCONNECT_1X03, 2.54mm_Pin_Headers:Interconnect_1x03, F.Cu at (108.0, 87.6)
- added J11: INTERCONNECT_1X03, 2.54mm_Pin_Headers:Interconnect_1x03, F.Cu at (34.3, 54.6)
- added J11: INTERCONNECT_1X03, 2.54mm_Pin_Headers:Interconnect_1x03, F.Cu at (108.0, 54.6)
- added J12: INTERCONNECT_1X03, 2.54mm_Pin_Headers:Interconnect_1x03, F.Cu at (34.3, 85.1)
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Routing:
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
